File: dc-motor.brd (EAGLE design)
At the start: 160 x 100 mm, 82 parts, among them IC1 MEGA32-A, X3 RIA_3POL, X4 RIA_3POL, X5 RIA_2POL, X6 JUMP1-4, X8 PFVERB10

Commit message: GND
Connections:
- net GND: now also IC1.13, IC1.19, IC1.37
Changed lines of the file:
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@@
 <contactref element="SV1" pad="11"/>
 <via x="128.27" y="59.69" extent="1-16" drill="0.7" shape="octagon"/>
+<contactref element="IC1" pad="13"/>
+<contactref element="IC1" pad="19"/>
+<contactref element="IC1" pad="37"/>
 </signal>
 <signal name="VDD">
@@
 <wire x1="60.96" y1="81.28" x2="64.135" y2="81.28" width="0.4064" layer="1"/>
 <via x="64.135" y="81.28" extent="1-16" drill="0.7" diameter="1.016" shape="octagon"/>
-<via x="71.755" y="81.28" extent="1-16" drill="0.7" diameter="1.016" shape="octagon"/>
-<wire x1="71.755" y1="81.28" x2="76.2" y2="81.28" width="0.4064" layer="1"/>
+<via x="72.0725" y="81.28" extent="1-16" drill="0.7" diameter="1.016" shape="octagon"/>
+<wire x1="72.0725" y1="81.28" x2="76.2" y2="81.28" width="0.4064" layer="1"/>
 <wire x1="76.2" y1="81.28" x2="76.835" y2="80.645" width="0.4064" layer="1"/>
 <wire x1="76.835" y1="80.645" x2="76.835" y2="71.755" width="0.4064" layer="1"/>
@@
 <wire x1="64.135" y1="81.28" x2="64.77" y2="81.28" width="0.4064" layer="16"/>
 <wire x1="64.77" y1="81.28" x2="66.04" y2="81.28" width="0.4064" layer="16"/>
-<wire x1="66.04" y1="81.28" x2="71.755" y2="81.28" width="0.4064" layer="16"/>
+<wire x1="66.04" y1="81.28" x2="72.0725" y2="81.28" width="0.4064" layer="16"/>
 <wire x1="15.875" y1="76.3144" x2="15.9789" y2="76.2105" width="0.4064" layer="1"/>
 <wire x1="13.3245" y1="76.2105" x2="11.4405" y2="76.2105" width="0.4064" layer="1"/>

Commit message: DC-DC Converter value added
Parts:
- R1: value (none) -> R785.0-0,5
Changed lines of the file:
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@@
 </element>
 <element name="C3" library="Capacitor" package="0805" value="100nF" x="74.6125" y="73.3425" rot="R270"/>
-<element name="R1" library="DC-DC-converter" package="SIP3" value="" x="53.34" y="5.08"/>
+<element name="R1" library="DC-DC-converter" package="SIP3" value="R785.0-0,5" x="53.34" y="5.08"/>
 <element name="C5" library="Capacitor" package="E5-13" value="47µF" x="41.91" y="8.89"/>
 <element name="C6" library="Capacitor" package="E5-13" value="100µF" x="70.485" y="8.89"/>

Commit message: Layout checked
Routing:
- net N$17: track 154.7 -> 153.8 mm
- net N$4: track 71.1 -> 71.9 mm
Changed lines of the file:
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@@
 <wire x1="100.6475" y1="66.9925" x2="101.6" y2="66.9925" width="0.4064" layer="1"/>
 <via x="101.6" y="66.9925" extent="1-16" drill="0.7" diameter="1.016" shape="octagon"/>
-<wire x1="101.6" y1="66.9925" x2="101.6" y2="45.085" width="0.4064" layer="16"/>
-<via x="101.6" y="45.085" extent="1-16" drill="0.7" diameter="1.016" shape="octagon"/>
-<wire x1="101.6" y1="45.085" x2="100.33" y2="45.085" width="0.4064" layer="1"/>
+<wire x1="101.6" y1="66.9925" x2="101.6" y2="45.72" width="0.4064" layer="16"/>
+<via x="101.6" y="45.72" extent="1-16" drill="0.7" diameter="1.016" shape="octagon"/>
+<wire x1="101.6" y1="45.72" x2="100.33" y2="45.72" width="0.4064" layer="1"/>
 <wire x1="91.44" y1="45.72" x2="90.17" y2="45.72" width="0.4064" layer="1"/>
 <wire x1="90.17" y1="45.72" x2="83.82" y2="45.72" width="0.4064" layer="1"/>
@@
 <wire x1="15.875" y1="80.01" x2="15.875" y2="76.3144" width="0.4064" layer="1"/>
 <wire x1="15.875" y1="76.3144" x2="15.9789" y2="76.2105" width="0.4064" layer="1"/>
-<wire x1="99.06" y1="45.72" x2="99.695" y2="45.085" width="0.4064" layer="1"/>
-<wire x1="99.695" y1="45.085" x2="100.33" y2="45.085" width="0.4064" layer="1"/>
+<wire x1="99.06" y1="45.72" x2="99.695" y2="45.72" width="0.4064" layer="1"/>
+<wire x1="99.695" y1="45.72" x2="100.33" y2="45.72" width="0.4064" layer="1"/>
 <wire x1="99.06" y1="45.72" x2="90.17" y2="45.72" width="0.4064" layer="1"/>
 </signal>
@@
 <wire x1="32.7025" y1="60.96" x2="32.7025" y2="60.6425" width="0.4064" layer="16"/>
 <via x="32.7025" y="60.6425" extent="1-16" drill="0.7" shape="octagon"/>
-<wire x1="32.7025" y1="60.6425" x2="32.7025" y2="53.975" width="0.4064" layer="1"/>
-<via x="32.7025" y="53.975" extent="1-16" drill="0.7" shape="octagon"/>
-<wire x1="32.7025" y1="53.975" x2="32.7025" y2="38.735" width="0.4064" layer="16"/>
+<wire x1="32.7025" y1="60.6425" x2="32.7025" y2="54.61" width="0.4064" layer="1"/>
+<via x="32.7025" y="54.61" extent="1-16" drill="0.7" shape="octagon"/>
+<wire x1="32.7025" y1="54.61" x2="32.7025" y2="38.735" width="0.4064" layer="16"/>
 <wire x1="94.2975" y1="47.625" x2="96.2959" y2="47.625" width="0.4064" layer="1"/>
 <wire x1="96.2959" y1="47.625" x2="96.3064" y2="47.6355" width="0.4064" layer="1"/>
@@
 <wire x1="33.81375" y1="38.89375" x2="33.655" y2="39.0525" width="0.4064" layer="16"/>
 <contactref element="SV1" pad="7"/>
-<wire x1="26.014" y1="71.173" x2="32.967" y2="71.173" width="0.4064" layer="16"/>
-<via x="34.29" y="71.12" extent="1-16" drill="0.6" shape="octagon"/>
-<wire x1="34.29" y1="71.12" x2="34.29" y2="64.4525" width="0.4064" layer="1"/>
+<via x="34.29" y="69.215" extent="1-16" drill="0.6" shape="octagon"/>
+<wire x1="34.29" y1="69.215" x2="34.29" y2="64.4525" width="0.4064" layer="1"/>
 <wire x1="80.645" y1="31.4325" x2="91.7575" y2="31.4325" width="0.4064" layer="16"/>
 <wire x1="91.7575" y1="31.4325" x2="92.075" y2="31.75" width="0.4064" layer="16"/>
@@
 <wire x1="96.2025" y1="31.4325" x2="143.51" y2="31.4325" width="0.4064" layer="16"/>
 <wire x1="143.51" y1="31.4325" x2="143.66875" y2="31.27375" width="0.4064" layer="16"/>
-<wire x1="34.29" y1="64.4525" x2="34.29" y2="55.245" width="0.4064" layer="1"/>
-<via x="34.29" y="55.245" extent="1-16" drill="0.7" shape="octagon"/>
+<wire x1="34.29" y1="64.4525" x2="34.29" y2="54.61" width="0.4064" layer="1"/>
+<via x="34.29" y="54.61" extent="1-16" drill="0.7" shape="octagon"/>
 <wire x1="33.655" y1="39.37" x2="33.655" y2="39.0525" width="0.4064" layer="16"/>
 <wire x1="33.655" y1="39.0525" x2="33.81375" y2="38.89375" width="0.4064" layer="16"/>
-<wire x1="32.967" y1="71.173" x2="34.237" y2="71.173" width="0.4064" layer="16"/>
-<wire x1="34.237" y1="71.173" x2="34.29" y2="71.12" width="0.4064" layer="16"/>
-<wire x1="34.29" y1="55.245" x2="34.29" y2="53.34" width="0.4064" layer="16"/>
+<wire x1="34.29" y1="54.61" x2="34.29" y2="53.34" width="0.4064" layer="16"/>
 <wire x1="34.29" y1="53.34" x2="33.655" y2="52.705" width="0.4064" layer="16"/>
 <wire x1="33.655" y1="52.705" x2="33.655" y2="39.37" width="0.4064" layer="16"/>
+<wire x1="26.014" y1="71.173" x2="33.602" y2="71.173" width="0.4064" layer="16"/>
+<wire x1="33.602" y1="71.173" x2="34.29" y2="70.485" width="0.4064" layer="16"/>
+<wire x1="34.29" y1="70.485" x2="34.29" y2="69.215" width="0.4064" layer="16"/>
 </signal>
 <signal name="N$21">
@@
 <wire x1="65.32" y1="46.495" x2="59.5125" y2="46.495" width="0.4064" layer="1"/>
 <wire x1="59.5125" y1="46.495" x2="59.055" y2="46.0375" width="0.4064" layer="1"/>
-<wire x1="59.055" y1="46.0375" x2="57.785" y2="46.0375" width="0.4064" layer="1"/>
-<via x="57.785" y="46.0375" extent="1-16" drill="0.7" diameter="1.016" shape="octagon"/>
-<wire x1="57.785" y1="46.0375" x2="56.515" y2="47.3075" width="0.4064" layer="16"/>
+<wire x1="59.055" y1="46.0375" x2="56.515" y2="46.0375" width="0.4064" layer="1"/>
+<via x="56.515" y="46.0375" extent="1-16" drill="0.7" diameter="1.016" shape="octagon"/>
 <wire x1="56.515" y1="47.3075" x2="56.515" y2="62.23" width="0.4064" layer="16"/>
 <via x="56.515" y="62.23" extent="1-16" drill="0.7" diameter="1.016" shape="octagon"/>
@@
 <via x="57.785" y="69.5325" extent="1-16" drill="0.7" diameter="1.016" shape="octagon"/>
 <wire x1="57.785" y1="69.5325" x2="73.025" y2="69.5325" width="0.4064" layer="16"/>
+<wire x1="56.515" y1="47.3075" x2="56.515" y2="46.0375" width="0.4064" layer="16"/>
 </signal>
 <signal name="N$8">
@@
 <via x="39.37" y="52.3875" extent="1-16" drill="0.7" diameter="1.016" shape="octagon"/>
 <wire x1="39.37" y1="52.3875" x2="43.815" y2="52.3875" width="0.4064" layer="1"/>
-<wire x1="43.815" y1="52.3875" x2="44.1325" y2="52.07" width="0.4064" layer="1"/>
 <wire x1="39.6875" y1="52.705" x2="39.37" y2="52.3875" width="0.4064" layer="16"/>
 <wire x1="44.1325" y1="52.07" x2="65.295" y2="52.07" width="0.4064" layer="1"/>
 <wire x1="65.295" y1="52.07" x2="65.32" y2="52.095" width="0.4064" layer="1"/>
+<wire x1="43.815" y1="52.3875" x2="44.1325" y2="52.07" width="0.4064" layer="1"/>
 </signal>
 <signal name="SCK">
@@
 <wire x1="45.085" y1="40.005" x2="69.5325" y2="40.005" width="0.4064" layer="16"/>
 <wire x1="70.32" y1="43.095" x2="70.32" y2="40.1575" width="0.4064" layer="1"/>
+<via x="69.85" y="39.6875" extent="1-16" drill="0.6" shape="octagon"/>
+<wire x1="31.115" y1="57.785" x2="34.925" y2="57.785" width="0.4064" layer="16"/>
+<wire x1="69.5325" y1="40.005" x2="69.85" y2="39.6875" width="0.4064" layer="16"/>
 <wire x1="70.32" y1="40.1575" x2="69.85" y2="39.6875" width="0.4064" layer="1"/>
-<via x="69.85" y="39.6875" extent="1-16" drill="0.6" shape="octagon"/>
-<wire x1="69.5325" y1="40.005" x2="69.85" y2="39.6875" width="0.4064" layer="16"/>
-<wire x1="31.115" y1="57.785" x2="34.925" y2="57.785" width="0.4064" layer="16"/>
 </signal>
 <signal name="RGB_BLAU">

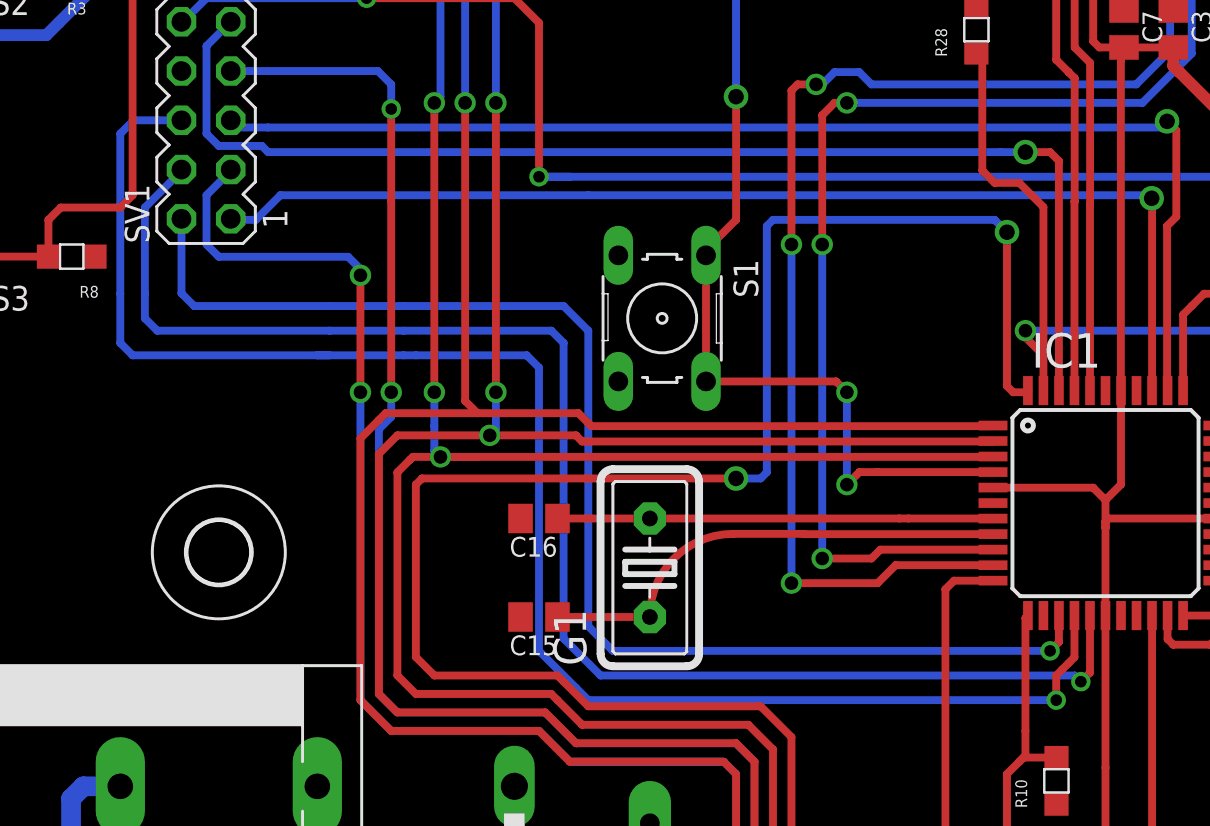
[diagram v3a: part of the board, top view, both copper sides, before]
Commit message: RGB_LED killed
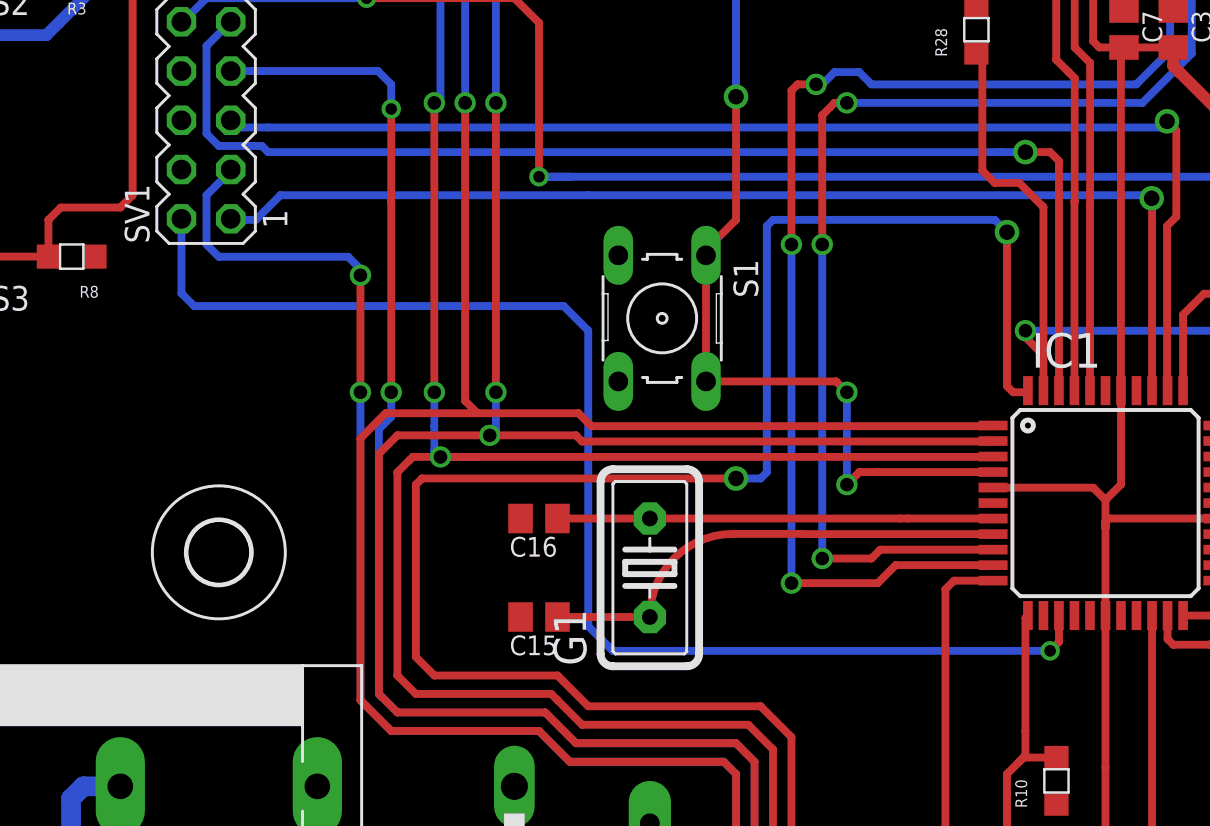
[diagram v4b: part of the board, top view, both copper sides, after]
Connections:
- net RGB_GRUEN renamed LED_YELLOW
- removed net RGB_BLAU: IC1.15, SV1.6
- removed net RGB_ROT: IC1.16, SV1.4
- net GND: now also IC1.15, IC1.16
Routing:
- net RGB_BLAU: track 84.1 -> 0.00 mm, vias 1 -> 0
- net RGB_ROT: track 77.0 -> 0.00 mm, vias 1 -> 0
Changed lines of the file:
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@@
 <layers>
 <layer number="1" name="Top" color="4" fill="1" visible="yes" active="yes"/>
-<layer number="2" name="Route2" color="1" fill="3" visible="yes" active="yes"/>
+<layer number="2" name="Route2" color="1" fill="3" visible="no" active="yes"/>
 <layer number="3" name="Route3" color="4" fill="3" visible="no" active="yes"/>
 <layer number="16" name="Bottom" color="1" fill="1" visible="yes" active="yes"/>
@@
 <contactref element="IC1" pad="19"/>
 <contactref element="IC1" pad="37"/>
+<contactref element="IC1" pad="16"/>
+<contactref element="IC1" pad="15"/>
 </signal>
 <signal name="VDD">
@@
 <wire x1="83.5025" y1="32.7025" x2="83.185" y2="33.02" width="0.4064" layer="16"/>
 </signal>
-<signal name="RGB_ROT">
-<contactref element="IC1" pad="16"/>
-<contactref element="SV1" pad="4"/>
-<wire x1="23.474" y1="66.093" x2="23.474" y2="66.019" width="0.4064" layer="16"/>
-<wire x1="23.474" y1="66.019" x2="21.59" y2="64.135" width="0.4064" layer="16"/>
-<wire x1="21.59" y1="64.135" x2="21.59" y2="59.69" width="0.4064" layer="16"/>
-<wire x1="21.59" y1="59.69" x2="21.59" y2="58.42" width="0.4064" layer="16"/>
-<wire x1="21.59" y1="58.42" x2="22.225" y2="57.785" width="0.4064" layer="16"/>
-<wire x1="22.225" y1="57.785" x2="31.115" y2="57.785" width="0.4064" layer="16"/>
-<wire x1="34.925" y1="57.785" x2="42.545" y2="57.785" width="0.4064" layer="16"/>
-<wire x1="42.545" y1="57.785" x2="43.18" y2="57.15" width="0.4064" layer="16"/>
-<wire x1="43.18" y1="57.15" x2="43.18" y2="41.91" width="0.4064" layer="16"/>
-<wire x1="43.18" y1="41.91" x2="45.085" y2="40.005" width="0.4064" layer="16"/>
-<wire x1="45.085" y1="40.005" x2="69.5325" y2="40.005" width="0.4064" layer="16"/>
-<wire x1="70.32" y1="43.095" x2="70.32" y2="40.1575" width="0.4064" layer="1"/>
-<via x="69.85" y="39.6875" extent="1-16" drill="0.6" shape="octagon"/>
-<wire x1="31.115" y1="57.785" x2="34.925" y2="57.785" width="0.4064" layer="16"/>
-<wire x1="69.5325" y1="40.005" x2="69.85" y2="39.6875" width="0.4064" layer="16"/>
-<wire x1="70.32" y1="40.1575" x2="69.85" y2="39.6875" width="0.4064" layer="1"/>
-</signal>
-<signal name="RGB_BLAU">
-<contactref element="IC1" pad="15"/>
-<contactref element="SV1" pad="6"/>
-<wire x1="23.474" y1="68.633" x2="21.008" y2="68.633" width="0.4064" layer="16"/>
-<wire x1="21.008" y1="68.633" x2="20.32" y2="67.945" width="0.4064" layer="16"/>
-<wire x1="20.32" y1="67.945" x2="20.32" y2="59.69" width="0.4064" layer="16"/>
-<via x="68.58" y="38.735" extent="1-16" drill="0.6" shape="octagon"/>
-<wire x1="43.815" y1="39.37" x2="41.91" y2="41.275" width="0.4064" layer="16"/>
-<wire x1="41.91" y1="41.275" x2="41.91" y2="55.88" width="0.4064" layer="16"/>
-<wire x1="41.91" y1="55.88" x2="41.275" y2="56.515" width="0.4064" layer="16"/>
-<wire x1="41.275" y1="56.515" x2="35.56" y2="56.515" width="0.4064" layer="16"/>
-<wire x1="35.56" y1="56.515" x2="34.925" y2="56.515" width="0.4064" layer="16"/>
-<wire x1="20.32" y1="59.69" x2="20.32" y2="57.15" width="0.4064" layer="16"/>
-<wire x1="20.32" y1="57.15" x2="20.955" y2="56.515" width="0.4064" layer="16"/>
-<wire x1="20.955" y1="56.515" x2="30.48" y2="56.515" width="0.4064" layer="16"/>
-<wire x1="30.48" y1="56.515" x2="31.115" y2="56.515" width="0.4064" layer="16"/>
-<wire x1="69.52" y1="43.095" x2="69.52" y2="40.945" width="0.4064" layer="1"/>
-<wire x1="69.52" y1="40.945" x2="69.215" y2="40.64" width="0.4064" layer="1"/>
-<wire x1="69.215" y1="40.64" x2="68.8975" y2="40.3225" width="0.4064" layer="1"/>
-<wire x1="68.8975" y1="40.3225" x2="68.58" y2="40.005" width="0.4064" layer="1"/>
-<wire x1="68.58" y1="40.005" x2="68.58" y2="38.735" width="0.4064" layer="1"/>
-<wire x1="43.815" y1="39.37" x2="44.45" y2="38.735" width="0.4064" layer="16"/>
-<wire x1="44.45" y1="38.735" x2="68.58" y2="38.735" width="0.4064" layer="16"/>
-<wire x1="34.925" y1="56.515" x2="30.48" y2="56.515" width="0.4064" layer="16"/>
-</signal>
-<signal name="RGB_GRUEN">
-<contactref element="IC1" pad="14"/>
-<contactref element="SV1" pad="2"/>
-<wire x1="23.474" y1="63.553" x2="23.474" y2="59.711" width="0.4064" layer="16"/>
-<wire x1="23.474" y1="59.711" x2="23.495" y2="59.69" width="0.4064" layer="16"/>
-<wire x1="23.495" y1="59.69" x2="24.13" y2="59.055" width="0.4064" layer="16"/>
-<wire x1="24.13" y1="59.055" x2="31.115" y2="59.055" width="0.4064" layer="16"/>
-<wire x1="34.925" y1="59.055" x2="43.18" y2="59.055" width="0.4064" layer="16"/>
-<wire x1="43.18" y1="59.055" x2="44.45" y2="57.785" width="0.4064" layer="16"/>
-<wire x1="44.45" y1="57.785" x2="44.45" y2="42.545" width="0.4064" layer="16"/>
-<wire x1="44.45" y1="42.545" x2="45.72" y2="41.275" width="0.4064" layer="16"/>
-<wire x1="45.72" y1="41.275" x2="68.2625" y2="41.275" width="0.4064" layer="16"/>
-<wire x1="68.72" y1="43.095" x2="68.72" y2="41.7325" width="0.4064" layer="1"/>
-<wire x1="68.72" y1="41.7325" x2="68.2625" y2="41.275" width="0.4064" layer="1"/>
-<via x="68.2625" y="41.275" extent="1-16" drill="0.6" shape="octagon"/>
-<wire x1="31.115" y1="59.055" x2="34.925" y2="59.055" width="0.4064" layer="16"/>
-</signal>
 <signal name="+24V_LED_µC">
 <contactref element="SV1" pad="8"/>
@@
 <wire x1="66.9925" y1="57.4425" x2="67.92" y2="56.515" width="0.4064" layer="1"/>
 </signal>
+<signal name="LED_YELLOW">
+<contactref element="SV1" pad="2"/>
+<contactref element="IC1" pad="14"/>
+<wire x1="23.474" y1="59.711" x2="23.495" y2="59.69" width="0.4064" layer="16"/>
+<wire x1="23.495" y1="59.69" x2="24.13" y2="59.055" width="0.4064" layer="16"/>
+<wire x1="24.13" y1="59.055" x2="31.115" y2="59.055" width="0.4064" layer="16"/>
+<wire x1="34.925" y1="59.055" x2="43.18" y2="59.055" width="0.4064" layer="16"/>
+<wire x1="43.18" y1="59.055" x2="44.45" y2="57.785" width="0.4064" layer="16"/>
+<wire x1="44.45" y1="57.785" x2="44.45" y2="42.545" width="0.4064" layer="16"/>
+<wire x1="44.45" y1="42.545" x2="45.72" y2="41.275" width="0.4064" layer="16"/>
+<wire x1="45.72" y1="41.275" x2="68.2625" y2="41.275" width="0.4064" layer="16"/>
+<wire x1="68.72" y1="43.095" x2="68.72" y2="41.7325" width="0.4064" layer="1"/>
+<wire x1="68.72" y1="41.7325" x2="68.2625" y2="41.275" width="0.4064" layer="1"/>
+<via x="68.2625" y="41.275" extent="1-16" drill="0.6" shape="octagon"/>
+<wire x1="31.115" y1="59.055" x2="34.925" y2="59.055" width="0.4064" layer="16"/>
+<wire x1="23.474" y1="59.711" x2="23.474" y2="63.553" width="0.4064" layer="16"/>
+</signal>
 </signals>

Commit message: Piggyboard & Board updated
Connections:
- net LED_YELLOW renamed ERROR_LED
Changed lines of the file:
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@@
 <wire x1="66.9925" y1="57.4425" x2="67.92" y2="56.515" width="0.4064" layer="1"/>
 </signal>
-<signal name="LED_YELLOW">
+<signal name="ERROR_LED">
 <contactref element="SV1" pad="2"/>
 <contactref element="IC1" pad="14"/>
